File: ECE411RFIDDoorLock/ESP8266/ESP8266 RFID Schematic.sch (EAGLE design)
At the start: 30 parts, among them M1 SERVO, Q3 DMG341, T1 600mA/40V, T2 600mA/40V, U3 AP2112-3.3, X1 ESP-12E, X4 20329

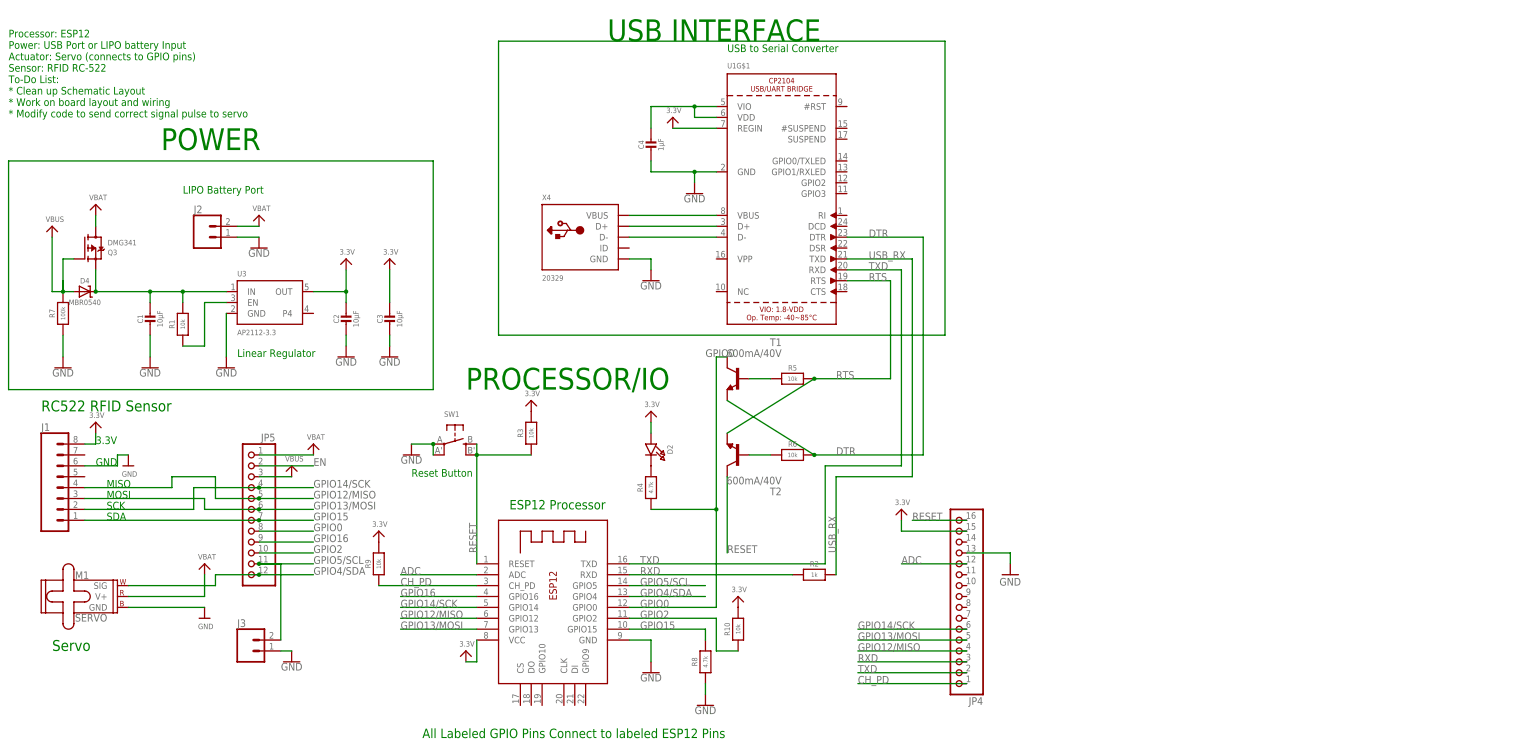
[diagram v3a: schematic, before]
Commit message: cleaned up some of the errors. Need to route 3.3V
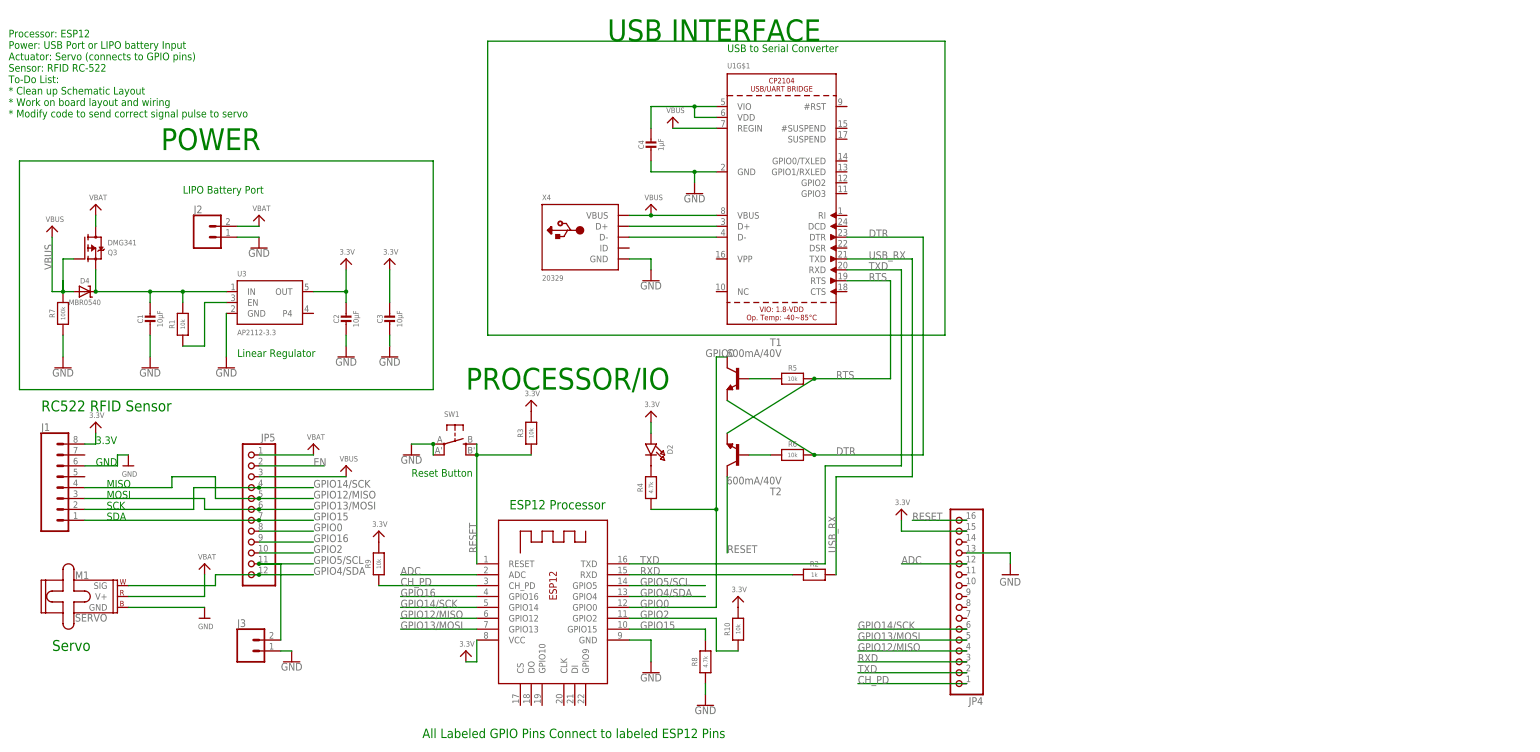
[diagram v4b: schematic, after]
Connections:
- removed net N$2: U1G$1.VBUS, X4.VBUS
- removed net N$9: D4.A, Q3.G, R7.2
- net 3.3V: no longer U1G$1.REGIN
- net VBUS: now also D4.A, Q3.G, R7.2, U1G$1.REGIN, U1G$1.VBUS, X4.VBUS
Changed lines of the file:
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@@
 </variantdefs>
 <classes>
-<class number="0" name="default" width="0" drill="0">
+<class number="0" name="default" width="0.3048" drill="0">
 </class>
-<class number="1" name="power" width="0.3048" drill="0">
+<class number="1" name="power" width="0.508" drill="0">
+</class>
+<class number="2" name="ground" width="0.3048" drill="0">
 </class>
 </classes>
@@
 <part name="GND6" library="SparkFun-PowerSymbols" deviceset="GND" device=""/>
 <part name="GND7" library="SparkFun-PowerSymbols" deviceset="GND" device=""/>
-<part name="U$10" library="microbuilder" deviceset="3.3V" device=""/>
 <part name="C4" library="microbuilder" deviceset="CAP_CERAMIC" device="0603MINI" value="1µF"/>
 <part name="R4" library="microbuilder" deviceset="RESISTOR" device="0603MINI" value="4.7k"/>
@@
 <part name="R10" library="microbuilder" deviceset="RESISTOR" device="0603MINI" value="10k"/>
 <part name="U$12" library="microbuilder" deviceset="3.3V" device=""/>
+<part name="U$13" library="microbuilder" deviceset="VBUS" device=""/>
+<part name="U$10" library="microbuilder" deviceset="VBUS" device=""/>
 </parts>
 <sheets>
@@
 <attribute name="VALUE" x="170.18" y="131.826" size="1.778" layer="96" align="top-center"/>
 </instance>
-<instance part="U$10" gate="G$1" x="165.1" y="149.86" smashed="yes">
-<attribute name="VALUE" x="163.576" y="150.876" size="1.27" layer="96"/>
-</instance>
 <instance part="C4" gate="G$1" x="160.02" y="142.24" smashed="yes">
 <attribute name="NAME" x="157.73" y="143.49" size="1.27" layer="95" font="vector" rot="R90" align="center"/>
@@
 <attribute name="VALUE" x="134.62" y="111.76" size="1.27" layer="96"/>
 </instance>
-<instance part="U$19" gate="G$1" x="76.2" y="68.58" smashed="yes">
-<attribute name="VALUE" x="74.676" y="69.596" size="1.27" layer="96"/>
+<instance part="U$19" gate="G$1" x="88.9" y="68.58" smashed="yes">
+<attribute name="VALUE" x="87.376" y="69.596" size="1.27" layer="96"/>
 </instance>
 <instance part="U$20" gate="G$1" x="81.28" y="73.66" smashed="yes">
@@
 <instance part="U$12" gate="G$1" x="180.34" y="38.1" smashed="yes">
 <attribute name="VALUE" x="178.816" y="39.116" size="1.27" layer="96"/>
+</instance>
+<instance part="U$13" gate="G$1" x="160.02" y="129.54" smashed="yes">
+<attribute name="VALUE" x="158.496" y="130.556" size="1.27" layer="96"/>
+</instance>
+<instance part="U$10" gate="G$1" x="165.1" y="149.86" smashed="yes">
+<attribute name="VALUE" x="163.576" y="150.876" size="1.27" layer="96"/>
 </instance>
 </instances>
@@
 </busses>
 <nets>
-<net name="VBAT" class="0">
+<net name="VBAT" class="1">
 <segment>
 <pinref part="U$2" gate="G$1" pin="VBAT"/>
@@
 </segment>
 </net>
-<net name="VBUS" class="0">
+<net name="VBUS" class="1">
 <segment>
 <pinref part="U$19" gate="G$1" pin="VBUS"/>
-<wire x1="68.58" y1="66.04" x2="76.2" y2="66.04" width="0.1524" layer="91"/>
+<wire x1="68.58" y1="66.04" x2="88.9" y2="66.04" width="0.1524" layer="91"/>
 <pinref part="JP5" gate="G$1" pin="3"/>
 </segment>
-</net>
-<net name="GND" class="0">
+<segment>
+<pinref part="R7" gate="G$1" pin="2"/>
+<wire x1="22.86" y1="109.22" x2="22.86" y2="111.76" width="0.1524" layer="91"/>
+<pinref part="Q3" gate="G$1" pin="G"/>
+<wire x1="25.4" y1="116.84" x2="22.86" y2="116.84" width="0.1524" layer="91"/>
+<wire x1="22.86" y1="116.84" x2="22.86" y2="109.22" width="0.1524" layer="91"/>
+<pinref part="U$1" gate="G$1" pin="VBUS"/>
+<wire x1="20.32" y1="121.92" x2="20.32" y2="109.22" width="0.1524" layer="91"/>
+<wire x1="20.32" y1="109.22" x2="22.86" y2="109.22" width="0.1524" layer="91"/>
+<pinref part="D4" gate="G$1" pin="A"/>
+<wire x1="25.4" y1="109.22" x2="22.86" y2="109.22" width="0.1524" layer="91"/>
+<junction x="22.86" y="109.22"/>
+<label x="20.32" y="114.3" size="1.778" layer="95" rot="R90"/>
+</segment>
+<segment>
+<pinref part="U1" gate="G$1" pin="VBUS"/>
+<wire x1="154.94" y1="127" x2="160.02" y2="127" width="0.1524" layer="91"/>
+<pinref part="X4" gate="G$1" pin="VBUS"/>
+<pinref part="U$13" gate="G$1" pin="VBUS"/>
+<wire x1="160.02" y1="127" x2="175.26" y2="127" width="0.1524" layer="91"/>
+<junction x="160.02" y="127"/>
+</segment>
+<segment>
+<pinref part="U1" gate="G$1" pin="REGIN"/>
+<wire x1="175.26" y1="147.32" x2="165.1" y2="147.32" width="0.1524" layer="91"/>
+<pinref part="U$10" gate="G$1" pin="VBUS"/>
+</segment>
+</net>
+<net name="GND" class="2">
 <segment>
 <pinref part="GND1" gate="1" pin="GND"/>
@@
 </segment>
 </net>
-<net name="3.3V" class="0">
+<net name="3.3V" class="1">
 <segment>
 <pinref part="U$6" gate="G$1" pin="3.3V"/>
@@
 <wire x1="27.94" y1="73.66" x2="30.48" y2="73.66" width="0.1524" layer="91"/>
 <wire x1="30.48" y1="73.66" x2="30.48" y2="76.2" width="0.1524" layer="91"/>
-</segment>
-<segment>
-<pinref part="U1" gate="G$1" pin="REGIN"/>
-<pinref part="U$10" gate="G$1" pin="3.3V"/>
-<wire x1="175.26" y1="147.32" x2="165.1" y2="147.32" width="0.1524" layer="91"/>
 </segment>
 <segment>
@@
 <pinref part="R10" gate="G$1" pin="2"/>
 <pinref part="U$12" gate="G$1" pin="3.3V"/>
-</segment>
-</net>
-<net name="N$2" class="0">
-<segment>
-<pinref part="U1" gate="G$1" pin="VBUS"/>
-<wire x1="154.94" y1="127" x2="175.26" y2="127" width="0.1524" layer="91"/>
-<pinref part="X4" gate="G$1" pin="VBUS"/>
 </segment>
 </net>
@@
 <net name="N$12" class="0">
 <segment>
-<wire x1="10.16" y1="139.7" x2="10.16" y2="86.36" width="0.1524" layer="91"/>
-<wire x1="10.16" y1="86.36" x2="109.22" y2="86.36" width="0.1524" layer="91"/>
 <wire x1="109.22" y1="86.36" x2="109.22" y2="139.7" width="0.1524" layer="91"/>
-<wire x1="109.22" y1="139.7" x2="10.16" y2="139.7" width="0.1524" layer="91"/>
+<wire x1="109.22" y1="86.36" x2="12.7" y2="86.36" width="0.1524" layer="91"/>
+<wire x1="12.7" y1="86.36" x2="12.7" y2="139.7" width="0.1524" layer="91"/>
+<wire x1="12.7" y1="139.7" x2="109.22" y2="139.7" width="0.1524" layer="91"/>
 </segment>
 </net>
 <net name="N$13" class="0">
 <segment>
-<wire x1="124.46" y1="99.06" x2="228.6" y2="99.06" width="0.1524" layer="91"/>
+<wire x1="121.92" y1="99.06" x2="228.6" y2="99.06" width="0.1524" layer="91"/>
 <wire x1="228.6" y1="99.06" x2="228.6" y2="167.64" width="0.1524" layer="91"/>
-<wire x1="228.6" y1="167.64" x2="124.46" y2="167.64" width="0.1524" layer="91"/>
-<wire x1="124.46" y1="167.64" x2="124.46" y2="99.06" width="0.1524" layer="91"/>
+<wire x1="228.6" y1="167.64" x2="121.92" y2="167.64" width="0.1524" layer="91"/>
+<wire x1="121.92" y1="167.64" x2="121.92" y2="99.06" width="0.1524" layer="91"/>
 </segment>
 </net>
@@
 </segment>
 </net>
-<net name="N$9" class="0">
-<segment>
-<pinref part="R7" gate="G$1" pin="2"/>
-<wire x1="22.86" y1="109.22" x2="22.86" y2="111.76" width="0.1524" layer="91"/>
-<pinref part="Q3" gate="G$1" pin="G"/>
-<wire x1="25.4" y1="116.84" x2="22.86" y2="116.84" width="0.1524" layer="91"/>
-<wire x1="22.86" y1="116.84" x2="22.86" y2="109.22" width="0.1524" layer="91"/>
-<pinref part="U$1" gate="G$1" pin="VBUS"/>
-<wire x1="20.32" y1="121.92" x2="20.32" y2="109.22" width="0.1524" layer="91"/>
-<wire x1="20.32" y1="109.22" x2="22.86" y2="109.22" width="0.1524" layer="91"/>
-<pinref part="D4" gate="G$1" pin="A"/>
-<wire x1="25.4" y1="109.22" x2="22.86" y2="109.22" width="0.1524" layer="91"/>
-<junction x="22.86" y="109.22"/>
-</segment>
-</net>
 <net name="N$10" class="0">
 <segment>
@@
 <net name="EN" class="0">
 <segment>
-<wire x1="81.28" y1="68.58" x2="68.58" y2="68.58" width="0.1524" layer="91"/>
+<wire x1="83.82" y1="68.58" x2="68.58" y2="68.58" width="0.1524" layer="91"/>
 <pinref part="JP5" gate="G$1" pin="2"/>
 <label x="81.28" y="68.58" size="1.778" layer="95"/>
@@
 </sheet>
 </sheets>
+<errors>
+</errors>
 </schematic>
 </drawing>

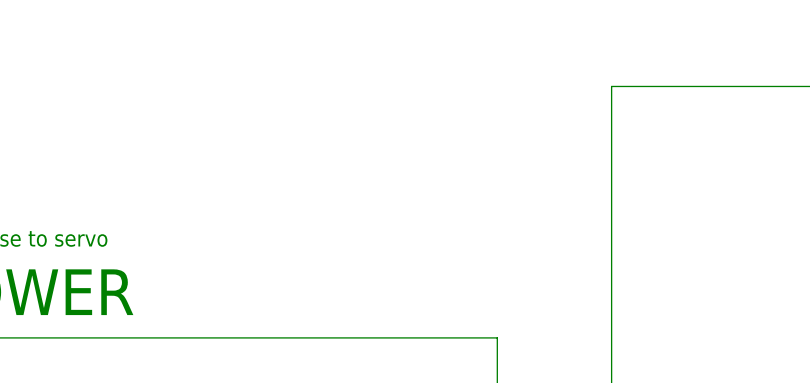
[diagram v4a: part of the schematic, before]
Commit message: Two ground planes, clean up, and power routing
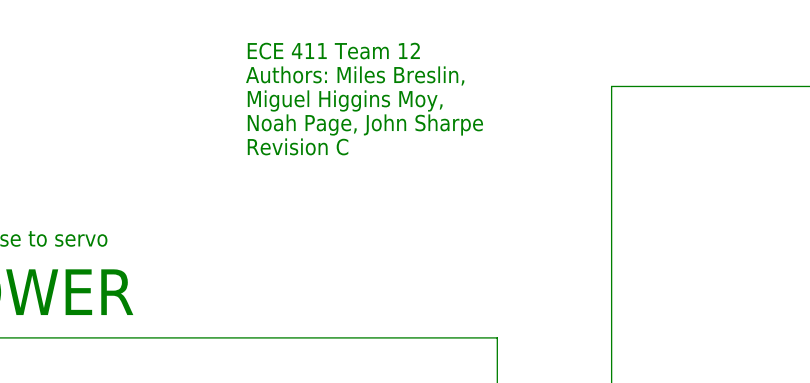
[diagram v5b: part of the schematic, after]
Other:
- note added: "ECE 411 Team 12 Authors: Miles Breslin, Miguel Higgins Moy, Noah Page, John Sharpe Revision C"
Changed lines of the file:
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@@
 <class number="2" name="ground" width="0.3048" drill="0">
+</class>
+<class number="3" name="battpower" width="1.27" drill="0">
 </class>
 </classes>
@@
 <text x="63.5" y="93.98" size="1.778" layer="91">Linear Regulator</text>
 <text x="50.8" y="132.08" size="1.778" layer="91">LIPO Battery Port</text>
+<text x="81.28" y="160.02" size="1.778" layer="91">ECE 411 Team 12
+Authors: Miles Breslin,
+Miguel Higgins Moy,
+Noah Page, John Sharpe
+Revision C</text>
 </plain>
 <instances>
@@
 </busses>
 <nets>
-<net name="VBAT" class="1">
+<net name="VBAT" class="3">
 <segment>
 <pinref part="U$2" gate="G$1" pin="VBAT"/>
